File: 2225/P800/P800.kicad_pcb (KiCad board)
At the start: 2 copper layers, 115 x 82.5 mm, 29 parts, among them J1 Screw_Terminal_01x05, J2 Conn_Coaxial, J3 Conn_Coaxial, J4 Conn_Coaxial, J5 Conn_Coaxial

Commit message: Completed initial P800 board layout.
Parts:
- HS1: value Heatsink_Pad -> Heatsink; footprint P800_footprint_library:heatsink_577202B04000G -> P800_footprint_library:heatsink_577202B00000G
- moved C802 75.7 mm to (104.5, 37.5), turned to -90 degrees
- moved R807 73.3 mm to (33.5, 70.5), turned to 180 degrees
- moved J5 72.6 mm to (41.0, 90.0), turned to 0 degrees
- moved R806 70.7 mm to (33.5, 61.5), turned to 90 degrees
- moved R801 63.3 mm to (69.5, 27.4), turned to 180 degrees
- moved R808 55.8 mm to (32.0, 78.0), turned to 180 degrees
- moved HS1 54.5 mm to (56.5, 67.8)
- moved R804 54.5 mm to (46.5, 47.5), turned to 90 degrees
- moved H805 54.5 mm to (59.0, 63.0)
- moved J4 52.5 mm to (29.5, 50.5), turned to -90 degrees
- moved C003 48.7 mm to (86.0, 65.0), turned to -90 degrees
- moved C002 48.7 mm to (86.0, 38.0), turned to -90 degrees
- moved J1 38.8 mm to (113.0, 65.9), turned to 90 degrees
- moved R803 35.5 mm to (62.0, 27.5)
- moved H807 31.5 mm to (67.0, 92.1), turned to 90 degrees
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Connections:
- C802 pad 1: Net-(C802-Pad1) -> /+24VAC
- F1 pad 1: /+24VAC -> Net-(J1-Pin_5)
- F1 pad 2: Net-(C802-Pad1) -> /+24VAC
- H803 pad 3: Net-(C802-Pad1) -> /+24VAC
- H804 pad 3: Net-(C802-Pad1) -> /+24VAC
- J1 pad 5: /+24VAC -> Net-(J1-Pin_5)
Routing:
- net GND: track 0.00 -> 425.7 mm, vias 0 -> 1
- net /-30VDC_out: track 0.00 -> 105.6 mm
- net /+30VDC_out: track 0.00 -> 86.1 mm
- net /+24VAC: track 0.00 -> 76.1 mm
- net /15VDC_out: track 0.00 -> 64.8 mm
- net Net-(H805-C): track 0.00 -> 49.2 mm
- net Net-(C805-Pad1): track 0.00 -> 48.2 mm, vias 0 -> 1
- net /-24VAC: track 0.00 -> 48.1 mm
- net Net-(H805-B): track 0.00 -> 41.7 mm
- net /35VDC_out: track 0.00 -> 36.9 mm
- net Net-(H806-B): track 0.00 -> 30.8 mm
- net Net-(J1-Pin_5): track 0.00 -> 25.8 mm
- net Net-(R806-Pad1): track 0.00 -> 17.7 mm
- net Net-(R807-Pad2): track 0.00 -> 7.54 mm
- added copper zone on B.Cu, net GND
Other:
- board size 115 x 82.5 mm -> 100 x 80 mm
- board text added: "+15VDC"
- board text added: "+30VDC"
- board text added: "+35VDC"
- board text added: "-30VDC"

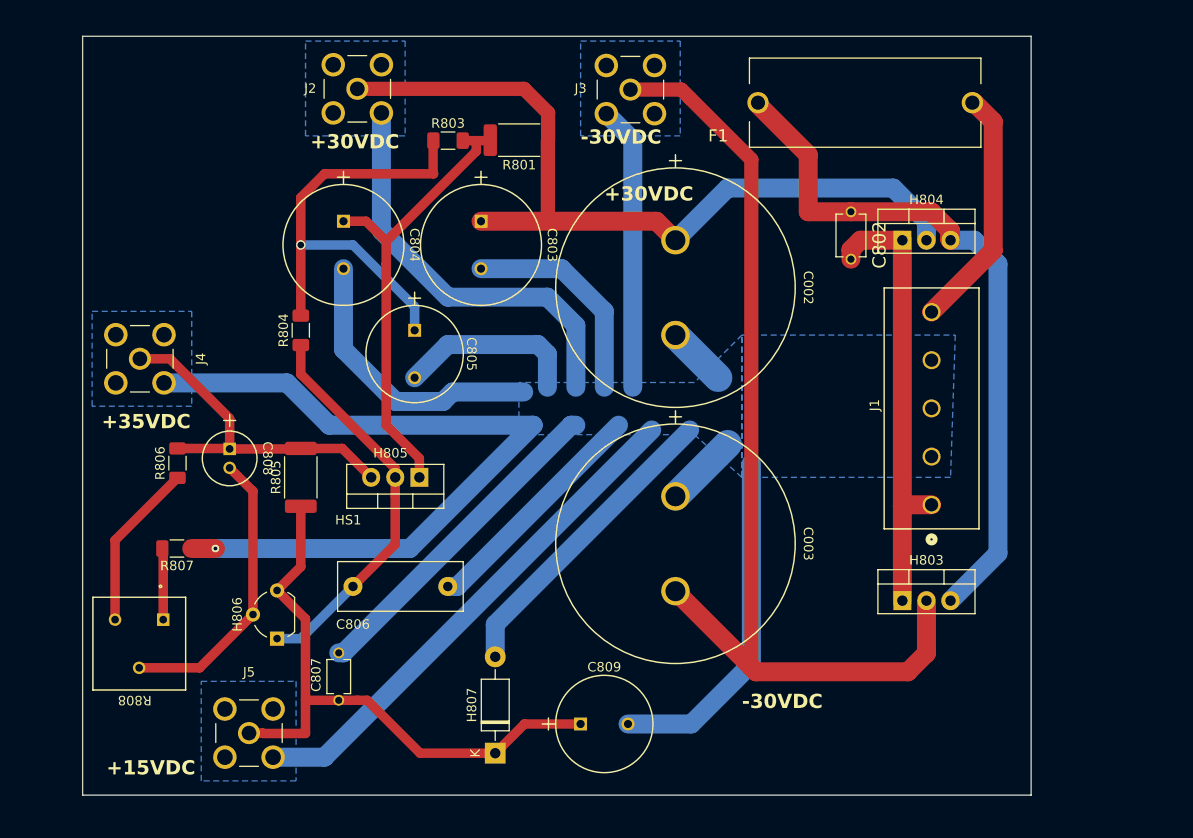
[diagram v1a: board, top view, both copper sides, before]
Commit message: Added screw mounting holes to 2225/P800 PCB
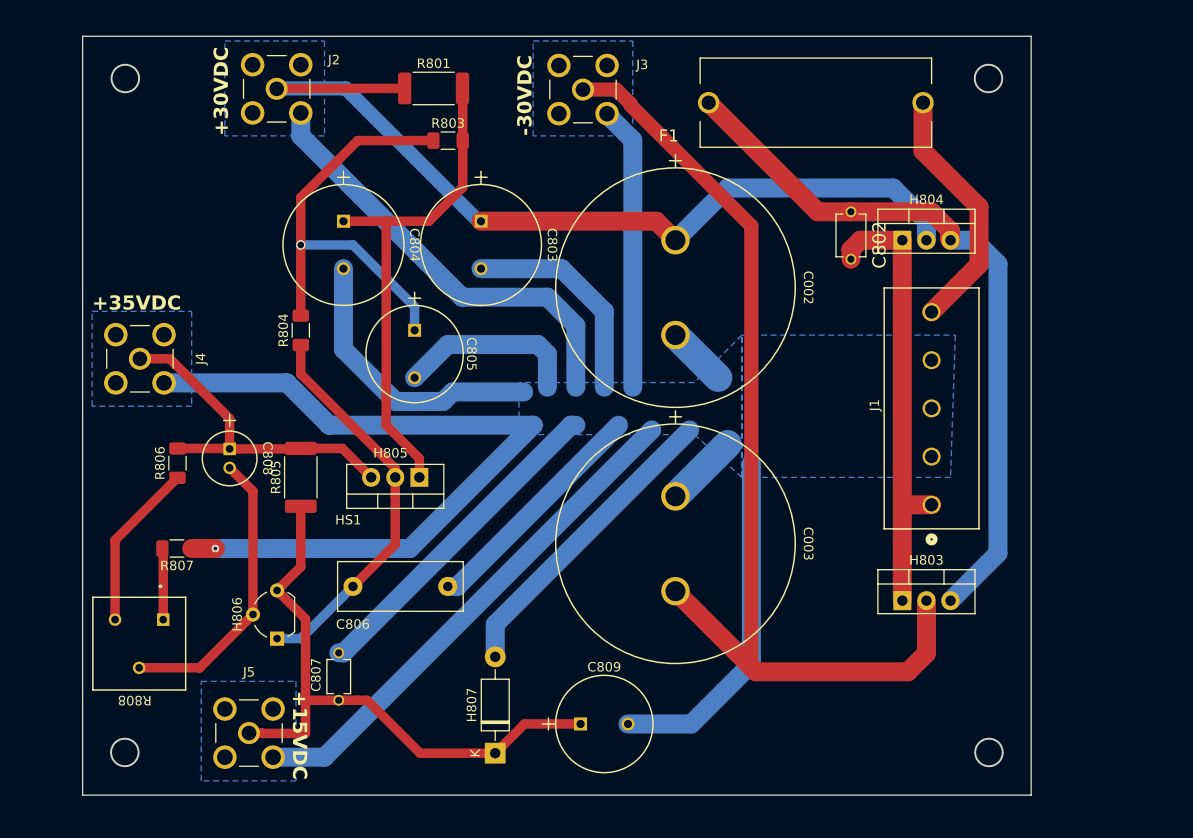
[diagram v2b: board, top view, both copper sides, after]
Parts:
- moved R801 10.5 mm to (60.5, 22.0), turned to 0 degrees
- moved J2 8.50 mm to (44.0, 22.0)
- moved F1 5.20 mm to (100.8, 23.5)
- moved J3 5.00 mm to (76.2, 22.1)
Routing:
- net /+30VDC_out: track 86.1 -> 94.5 mm
- net Net-(H805-C): track 49.2 -> 52.9 mm
- net GND: track 425.7 -> 428.3 mm
- net Net-(C805-Pad1): track 48.2 -> 46.1 mm
- net /+24VAC: track 76.1 -> 77.6 mm
- net /-30VDC_out: track 105.6 -> 106.6 mm
- net Net-(J1-Pin_5): track 25.8 -> 26.6 mm
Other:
- outline, holes or cut-outs redrawn

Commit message: Replaced custom capacitor footprints with kicad standard footprints
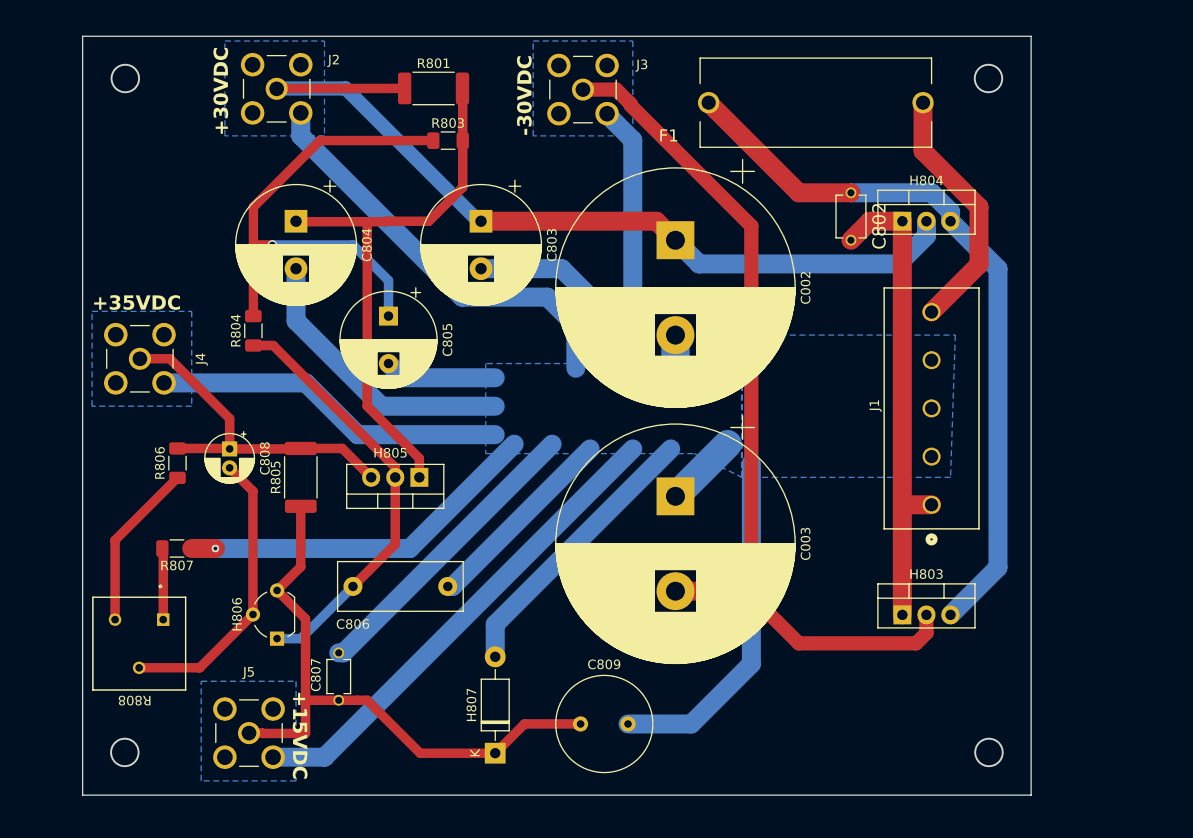
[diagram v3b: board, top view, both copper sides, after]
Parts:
- C002, C003: footprint P800_footprint_library:cap_electrolytic_A50 -> Capacitor_THT:CP_Radial_D25.0mm_P10.00mm_SnapIn
- C803, C804: footprint P800_footprint_library:cap_electrolytic_UKW1J471MHD1TO -> Capacitor_THT:CP_Radial_D12.5mm_P5.00mm
- C805: footprint P800_footprint_library:cap_electrolytic_UFG1H101MPM1TD -> Capacitor_THT:CP_Radial_D10.0mm_P5.00mm
- C808: footprint P800_footprint_library:cap_electrolytic_panasonic_5X11 -> Capacitor_THT:CP_Radial_D5.0mm_P2.00mm
- C809: footprint P800_footprint_library:cap_electrolytic_UFG1C471MPM1TD -> Capacitor_THT:C_Radial_D10.0mm_H20.0mm_P5.00mm
- moved R804 5.00 mm to (41.5, 47.5)
- moved C804 5.00 mm to (46.0, 36.0)
- moved C805 3.13 mm to (55.8, 46.0)
- moved C802 2.00 mm to (104.5, 35.5)
- moved H804 2.00 mm to (109.9, 36.0)
- moved H803 1.50 mm to (109.9, 77.5)
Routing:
- net GND: track 428.3 -> 393.6 mm
- net /-30VDC_out: track 106.6 -> 93.9 mm
- net Net-(C805-Pad1): track 46.1 -> 53.0 mm
- net Net-(H805-C): track 52.9 -> 58.8 mm
- net Net-(H805-B): track 41.7 -> 45.0 mm
- net /-24VAC: track 48.1 -> 50.9 mm
- net /+30VDC_out: track 94.5 -> 92.6 mm
- net /+24VAC: track 77.6 -> 76.9 mm

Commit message: Replaced star ground pattern with single ground plane
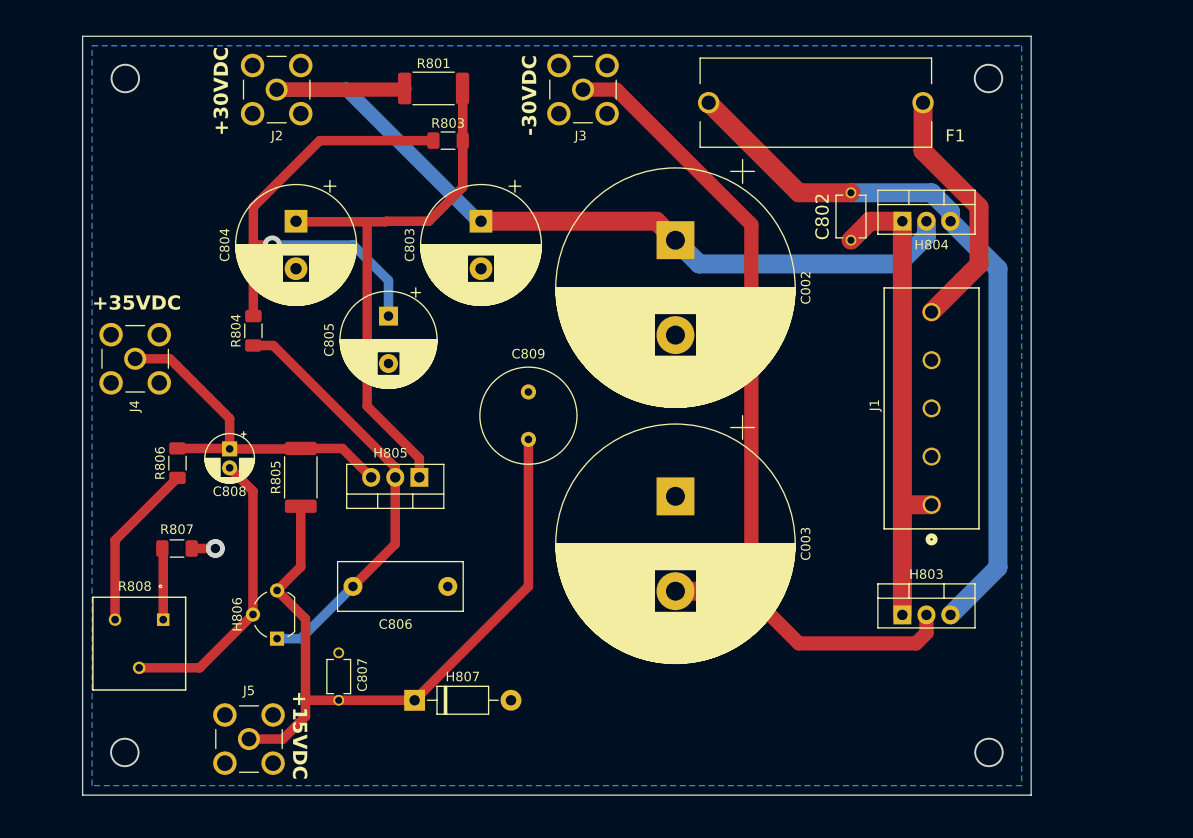
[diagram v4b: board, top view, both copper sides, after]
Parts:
- moved C809 30.5 mm to (70.5, 59.0), turned to 90 degrees
- moved H807 10.2 mm to (58.5, 86.5), turned to 0 degrees
- moved J5 0.63 mm to (41.0, 90.6)
- moved J4 0.50 mm to (29.0, 50.5)
- moved J2 0.08 mm to (44.0, 22.1)
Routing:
- net GND: track 393.6 -> 2.00 mm
- net /15VDC_out: track 64.8 -> 75.4 mm
- net /35VDC_out: track 36.9 -> 37.6 mm

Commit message: Made P800 PCB smaller
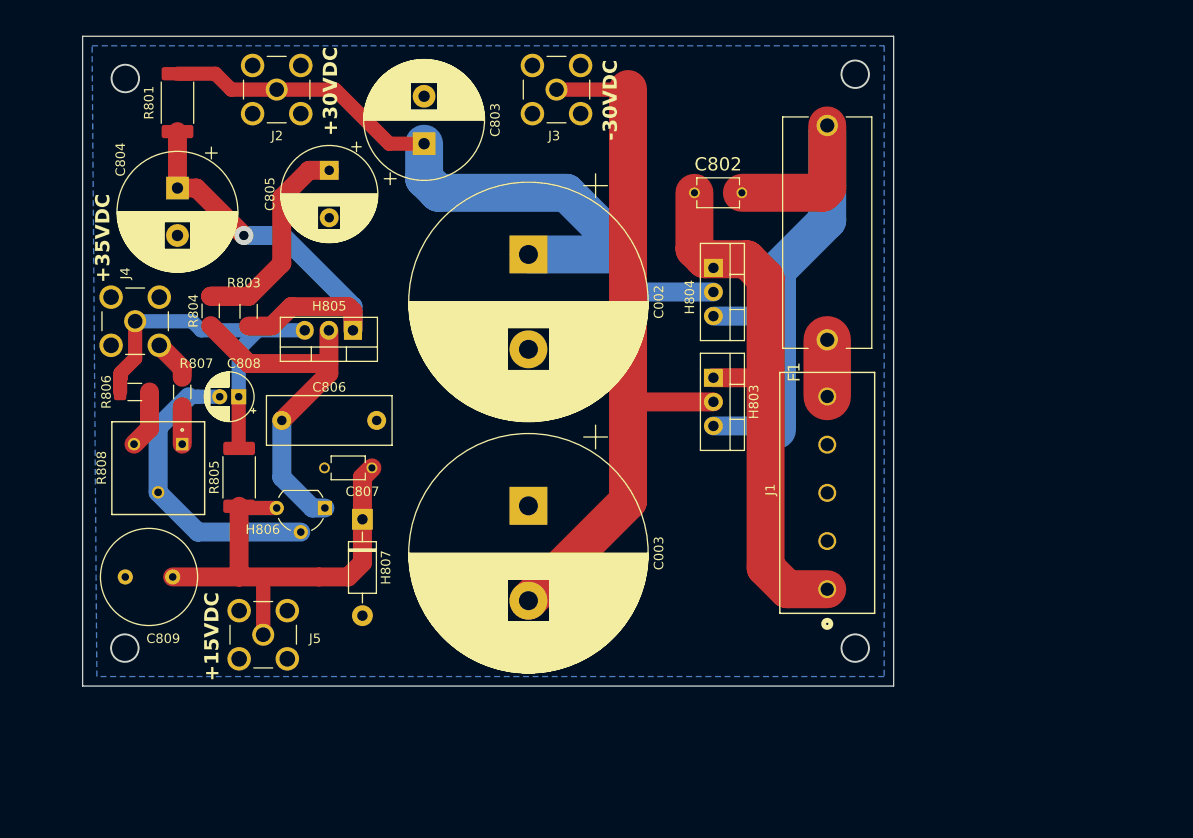
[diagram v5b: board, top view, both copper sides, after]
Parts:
- moved C809 40.2 mm to (33.0, 73.5), turned to 180 degrees
- moved H803 32.0 mm to (90.0, 52.5), turned to -90 degrees
- moved R803 27.7 mm to (41.0, 45.5), turned to -90 degrees
- moved R801 27.0 mm to (33.5, 23.5), turned to -90 degrees
- moved C807 22.0 mm to (51.5, 62.0), turned to 180 degrees
- moved H804 20.5 mm to (90.0, 40.9), turned to -90 degrees
- moved H807 19.9 mm to (53.0, 67.4), turned to -90 degrees
- moved C806 19.0 mm to (44.5, 57.0)
- moved R808 18.6 mm to (34.0, 59.5)
- moved HS1 17.0 mm to (49.5, 52.3)
- moved H805 17.0 mm to (52.0, 47.5)
- moved C805 16.6 mm to (49.5, 30.6)
- moved R807 16.5 mm to (34.0, 54.0), turned to -90 degrees
- moved C002 15.6 mm to (70.5, 39.5)
- moved C003 15.5 mm to (70.5, 66.0)
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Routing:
- net Net-(C805-Pad1): track 53.0 -> 24.7 mm, vias 1 -> 0
- net /15VDC_out: track 75.4 -> 48.7 mm
- net Net-(J1-Pin_5): track 26.6 -> 5.98 mm
- net /-30VDC_out: track 93.9 -> 73.6 mm
- net /+24VAC: track 76.9 -> 63.1 mm
- net Net-(H805-C): track 58.8 -> 46.1 mm, vias 0 -> 1
- net /+30VDC_out: track 92.9 -> 81.4 mm
- net Net-(R806-Pad1): track 17.7 -> 6.18 mm
- net Net-(H805-B): track 45.0 -> 37.5 mm
- net /-24VAC: track 50.9 -> 57.6 mm
- net Net-(R807-Pad2): track 7.54 -> 3.95 mm
- net GND: track 2.00 -> 4.37 mm, vias 1 -> 0
- net /35VDC_out: track 37.6 -> 39.7 mm
- net Net-(H806-B): track 30.8 -> 31.5 mm
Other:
- board size 100 x 80 mm -> 85.5 x 68.5 mm

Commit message: Redesigned P800 layout
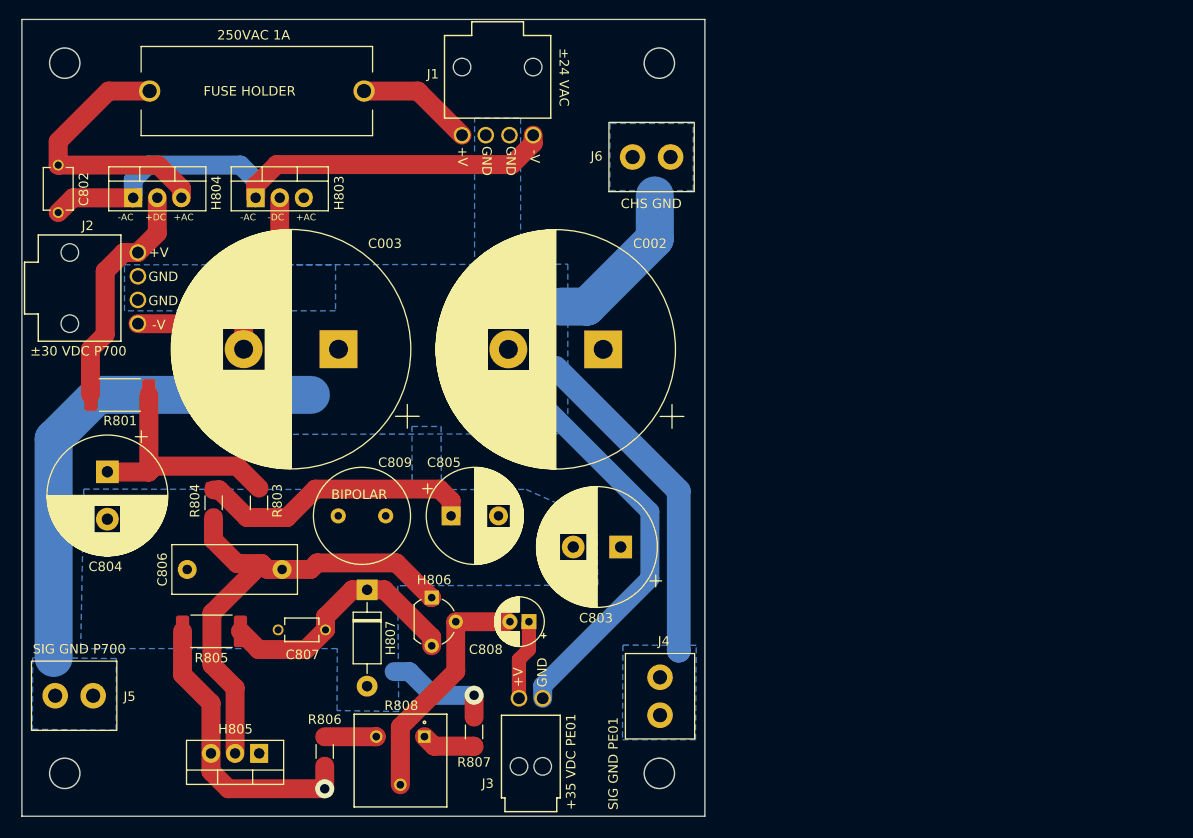
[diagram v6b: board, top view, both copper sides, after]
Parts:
- added J6: Conn_01x01, P800_footprint_library:Metz_Connect_1pos_terminal_360291, F.Cu at (83.5, 29.2)
- J1: value Screw_Terminal_01x05 -> Conn_01x04; footprint P800_footprint_library:molex_5pos_connector_395443005 -> P800_footprint_library:molex_nanofit_4-pos_header_1053131204
- J2: value Conn_Coaxial -> Conn_01x04; footprint P800_footprint_library:sma_connector_RFPC-SMA27-F -> P800_footprint_library:molex_nanofit_4-pos_header_1053131204
- J3: value Conn_Coaxial -> Conn_01x02; footprint P800_footprint_library:sma_connector_RFPC-SMA27-F -> P800_footprint_library:molex_nanofit_2-pos_header_1053132302
- J4, J5: value Conn_Coaxial -> Conn_01x01; footprint P800_footprint_library:sma_connector_RFPC-SMA27-F -> P800_footprint_library:Metz_Connect_1pos_terminal_360291
- moved C802 69.6 mm to (20.9, 32.6), turned to -90 degrees
- moved J4 68.0 mm to (84.4, 86.1), turned to 0 degrees
- moved J3 64.2 mm to (72.0, 86.3), turned to 0 degrees
- moved F1 62.0 mm to (41.9, 22.3), turned to 180 degrees
- moved H804 61.6 mm to (28.8, 33.5), turned to 0 degrees
- moved J1 61.4 mm to (63.5, 26.9), turned to 180 degrees
- moved H803 51.9 mm to (41.7, 33.5), turned to 0 degrees
- moved C803 47.3 mm to (80.2, 70.3), turned to 180 degrees
- moved R807 47.2 mm to (64.8, 89.8)
- moved HS1 46.1 mm to (39.7, 97.3)
- moved H805 45.7 mm to (42.1, 92.1)
- moved R806 42.9 mm to (49.0, 91.9), turned to -90 degrees
- moved R808 40.0 mm to (59.5, 90.3)
- moved C808 38.7 mm to (70.6, 78.2)
- moved C805 38.6 mm to (62.3, 67.1), turned to 0 degrees
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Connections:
- net Net-(H805-C) renamed /H805C_45V
- C802 pad 1: /+24VAC -> FBR AC +
- C807 pad 1: /15VDC_out -> Net-(H806-E)
- C808 pad 1: /35VDC_out -> /+35VDC_out
- C809 pad 1: /15VDC_out -> Net-(H806-E)
- F1 pad 1: Net-(J1-Pin_5) -> /+24VAC
- F1 pad 2: /+24VAC -> FBR AC +
- H803 pad 3: /+24VAC -> FBR AC +
- H804 pad 3: /+24VAC -> FBR AC +
- H805 pad 3: /35VDC_out -> /+35VDC_out
- H806 pad 3: /15VDC_out -> Net-(H806-E)
- H807 pad 1: /15VDC_out -> Net-(H806-E)
- J1 pad 1: /-24VAC -> /+24VAC
- J1 pad 4: GND -> /-24VAC
- J2 pad 1: /+30VDC_out -> /-30VDC_out
- J3 pad 1: /-30VDC_out -> GND
- J3 pad 2: GND -> /+35VDC_out
- J4 pad 1: /35VDC_out -> GND
- J5 pad 1: /15VDC_out -> GND
- R805 pad 1: /15VDC_out -> Net-(H806-E)
- R805 pad 2: /35VDC_out -> /+35VDC_out
- R806 pad 2: /35VDC_out -> /+35VDC_out
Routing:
- net GND: track 4.37 -> 156.3 mm, vias 0 -> 1
- net /+35VDC_out: track 0.00 -> 64.1 mm, vias 0 -> 1
- net /+24VAC: track 63.1 -> 12.3 mm
- net /15VDC_out: track 48.7 -> 0.00 mm
- net FBR AC +: track 0.00 -> 46.8 mm
- net /-30VDC_out: track 73.6 -> 31.0 mm
- net /35VDC_out: track 39.7 -> 0.00 mm
- net /+30VDC_out: track 81.4 -> 121.0 mm
- net Net-(H806-E): track 0.00 -> 36.0 mm
- net /H805C_45V: track 46.1 -> 67.7 mm, vias 1 -> 0
- net Net-(H805-B): track 37.5 -> 51.6 mm
- net Net-(H806-B): track 31.5 -> 25.0 mm
- net Net-(J1-Pin_5): track 5.98 -> 0.00 mm
- net Net-(C805-Pad1): track 24.7 -> 29.6 mm
- net /-24VAC: track 57.6 -> 59.8 mm
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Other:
- board size 85.5 x 68.5 mm -> 72 x 84 mm
- copper layers 2 -> 4
- board text added: "+35 VDC PE01"
- board text added: "+AC"
- board text added: "+DC"
- board text added: "+V"
- board text added: "-AC"
- board text added: "-DC"
- board text added: "-V"
- board text added: "250VAC 1A"
- board text added: "BIPOLAR"
- board text added: "CHS GND"
- board text added: "FUSE HOLDER"
- board text added: "GND"
- board text added: "SIG GND P700"
- board text added: "SIG GND PE01"
- board text added: "Spec dimensions: <80mm x <100mm Design dimensions: 72mm x 84mm"
- board text added: "±24 VAC"
- board text added: "±30 VDC P700"
- board text removed: "+15VDC"
- board text removed: "+30VDC"
- board text removed: "+35VDC"
- board text removed: "-30VDC"

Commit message: Changed molex connectors on P800 pcb from horizontal to vertical plug direction components
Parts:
- J1, J2: footprint P800_footprint_library:molex_nanofit_4-pos_header_1053131204 -> P800_footprint_library:molex_nanofit_4-pos_header_vert_1053091204
- J3: footprint P800_footprint_library:molex_nanofit_2-pos_header_1053132302 -> P800_footprint_library:molex_nanofit_2-pos_header_vert_1053091302
- moved J3 7.52 mm to (72.1, 93.8), turned to 180 degrees
- moved J2 7.35 mm to (22.0, 47.5), turned to 90 degrees
- moved J1 7.19 mm to (63.5, 19.7), turned to 0 degrees
- moved C802 4.39 mm to (20.9, 28.2)
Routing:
- net GND: track 156.3 -> 163.8 mm
- net /-24VAC: track 59.8 -> 66.5 mm
- net /-30VDC_out: track 31.0 -> 36.8 mm
- net FBR AC +: track 46.8 -> 41.1 mm
- net /+35VDC_out: track 64.1 -> 69.6 mm
- net /+30VDC_out: track 121.0 -> 125.4 mm
- net /+24VAC: track 12.3 -> 11.4 mm
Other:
- board text added: "24 VAC"
- board text added: "250 VAC 1A FUSE"
- board text removed: "250VAC 1A"
- board text removed: "±24 VAC"
